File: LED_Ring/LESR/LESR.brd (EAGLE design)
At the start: 40 x 40 mm, 32 parts, among them U1 APDS-9960, U2 NCP1117ST33T3G

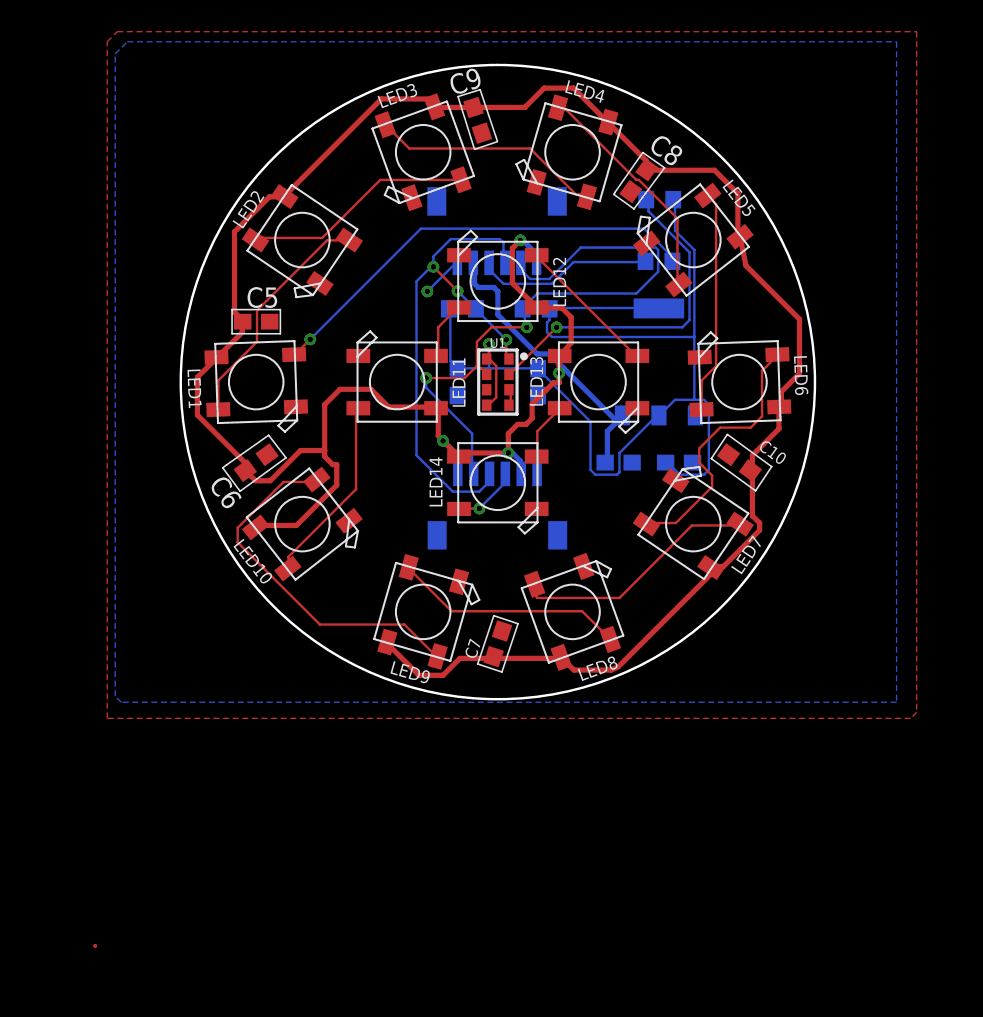
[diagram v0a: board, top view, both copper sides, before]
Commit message: 12V to 5V LDO version
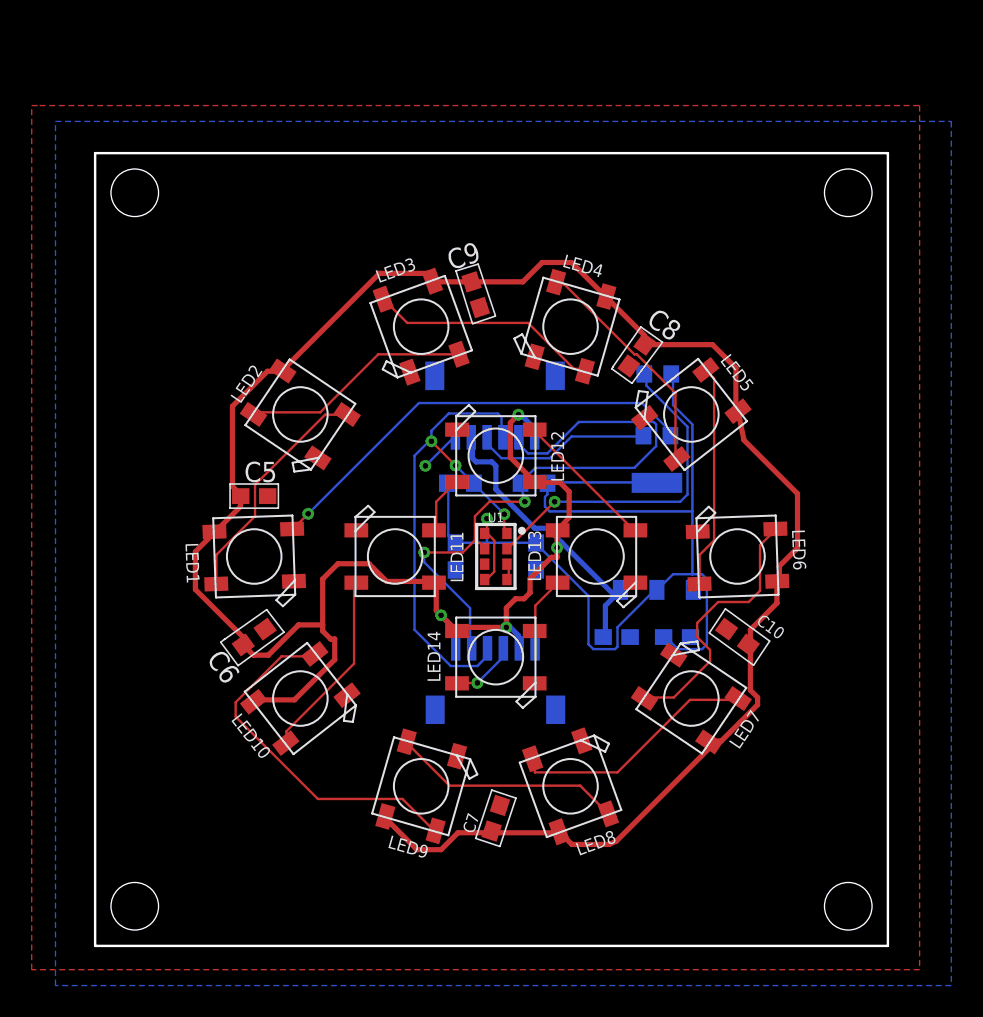
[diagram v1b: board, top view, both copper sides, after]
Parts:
- moved C2 11.0 mm to (27.8, 24.6)
- moved C4 11.0 mm to (22.7, 24.6)
- moved LED1 11.0 mm to (10.0, 24.6)
- moved LED11 11.0 mm to (18.9, 24.6)
- moved LED13 11.0 mm to (31.6, 24.6)
- moved LED6 11.0 mm to (40.5, 24.6)
- moved U1 11.0 mm to (25.3, 24.6)
- moved LED10 11.0 mm to (12.9, 15.6)
- moved LED7 11.0 mm to (37.6, 15.6)
- moved C1 11.0 mm to (32.9, 19.5)
- moved C10 11.0 mm to (40.5, 19.5)
- moved C3 11.0 mm to (36.7, 19.5)
- moved C6 11.0 mm to (10.0, 19.5)
- moved C7 11.0 mm to (25.3, 8.05)
- moved C8 11.0 mm to (34.2, 37.3)
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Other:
- board size 40 x 40 mm -> 50 x 50 mm
- board text added: "1"
- board text added: "5V"
- board text added: "6"
- board text added: "DIN"
- board text added: "GND"
- board text added: "SCL"
- board text added: "SDA"
